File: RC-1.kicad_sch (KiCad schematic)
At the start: 0 parts

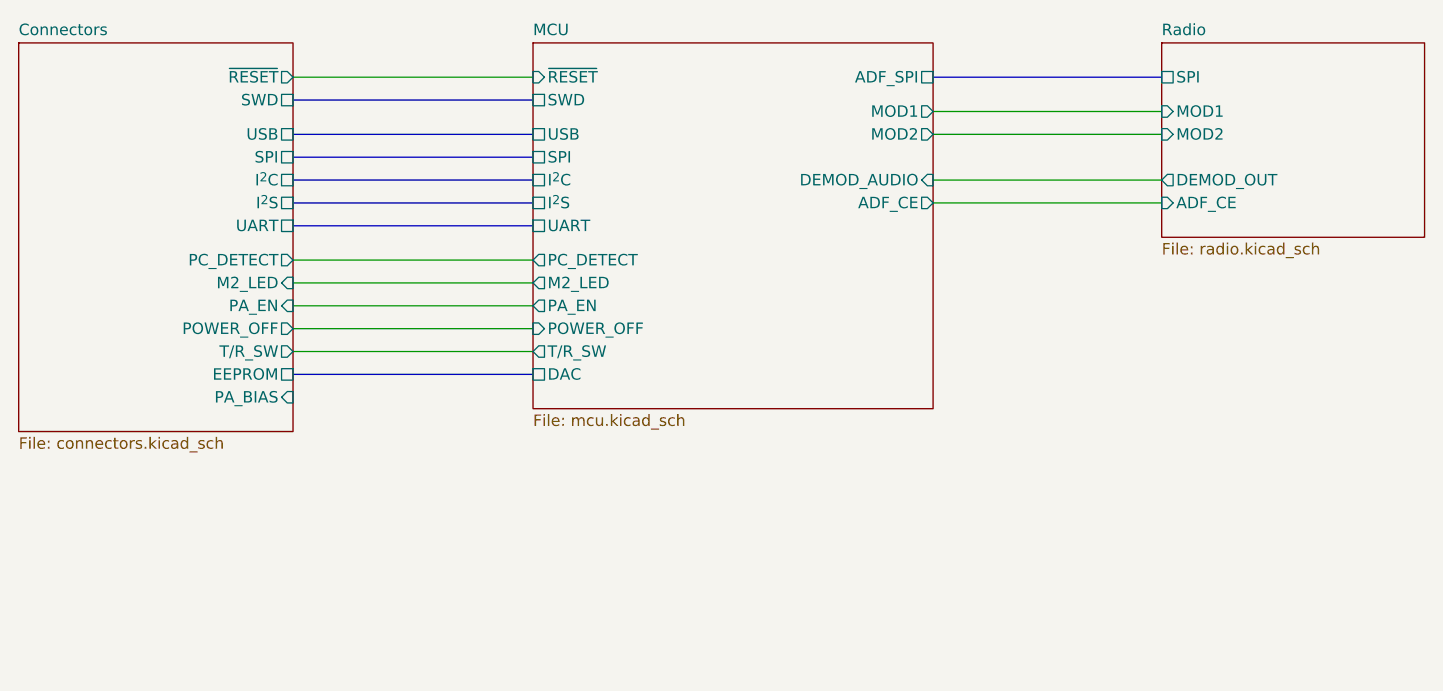
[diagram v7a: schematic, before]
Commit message: Added DAC for PA/preselector bias voltage
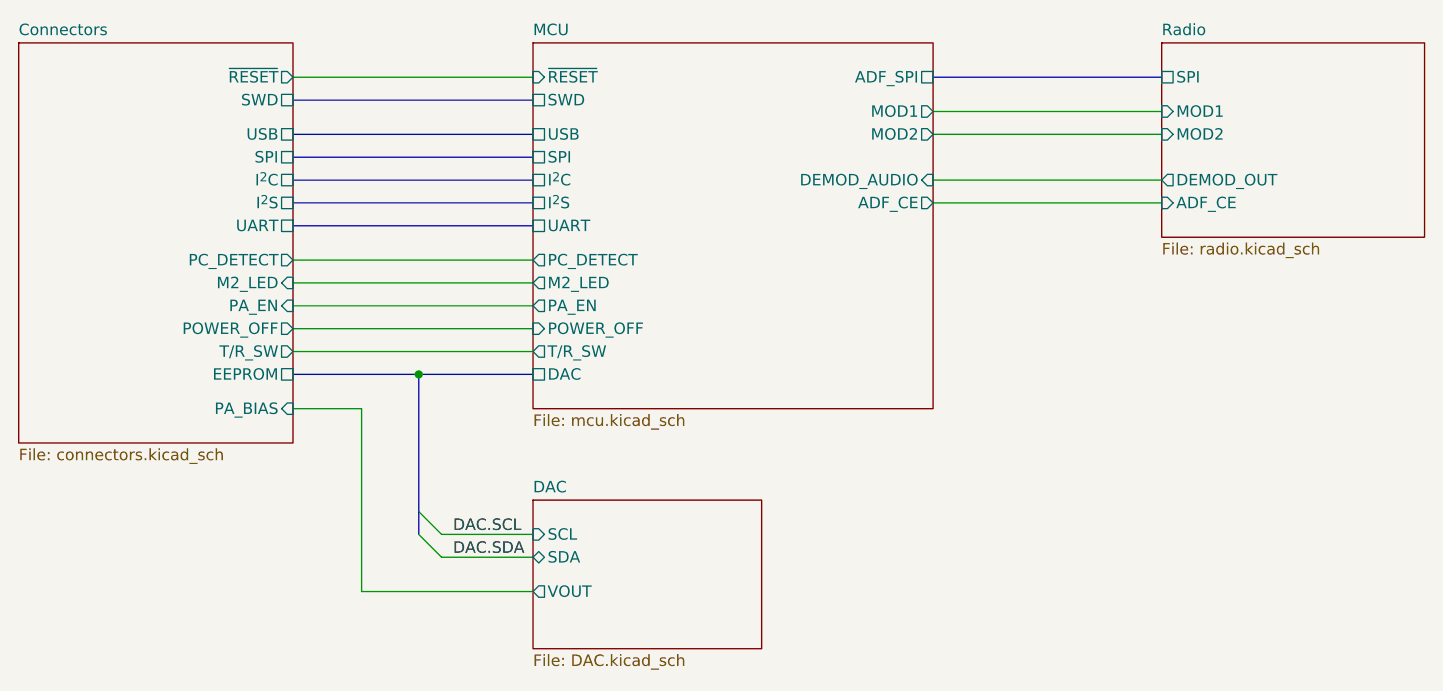
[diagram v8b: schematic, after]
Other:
- added sheet DAC (DAC.kicad_sch)
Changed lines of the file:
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@@
     (company "OpenRTX + M17")
   )
+  (junction (at 118.11 118.11) (diameter 0) (color 0 0 0 0)
+  )
+  (bus_entry (at 118.11 133.35) (size 2.54 2.54)
+    (stroke (width 0) (type default) (color 0 0 0 0))
+  )
+  (bus_entry (at 118.11 135.89) (size 2.54 2.54)
+    (stroke (width 0) (type default) (color 0 0 0 0))
+  )
   (bus (pts (xy 104.14 99.06) (xy 130.81 99.06))
     (stroke (width 0) (type default) (color 0 0 0 0))
   )
+  (wire (pts (xy 120.65 138.43) (xy 130.81 138.43))
+    (stroke (width 0) (type default) (color 0 0 0 0))
+  )
   (bus (pts (xy 104.14 87.63) (xy 130.81 87.63))
     (stroke (width 0) (type default) (color 0 0 0 0))
@@
     (stroke (width 0) (type default) (color 0 0 0 0))
   )
-  (bus (pts (xy 104.14 118.11) (xy 130.81 118.11))
+  (bus (pts (xy 104.14 118.11) (xy 118.11 118.11))
+    (stroke (width 0) (type default) (color 0 0 0 0))
+  )
+  (wire (pts (xy 111.76 121.92) (xy 111.76 142.24))
     (stroke (width 0) (type default) (color 0 0 0 0))
   )
@@
     (stroke (width 0) (type default) (color 0 0 0 0))
   )
+  (wire (pts (xy 111.76 142.24) (xy 130.81 142.24))
+    (stroke (width 0) (type default) (color 0 0 0 0))
+  )
   (wire (pts (xy 175.26 91.44) (xy 200.66 91.44))
     (stroke (width 0) (type default) (color 0 0 0 0))
@@
     (stroke (width 0) (type default) (color 0 0 0 0))
   )
+  (bus (pts (xy 118.11 118.11) (xy 130.81 118.11))
+    (stroke (width 0) (type default) (color 0 0 0 0))
+  )
+  (wire (pts (xy 120.65 135.89) (xy 130.81 135.89))
+    (stroke (width 0) (type default) (color 0 0 0 0))
+  )
+  (bus (pts (xy 118.11 133.35) (xy 118.11 135.89))
+    (stroke (width 0) (type default) (color 0 0 0 0))
+  )
   (bus (pts (xy 104.14 96.52) (xy 130.81 96.52))
     (stroke (width 0) (type default) (color 0 0 0 0))
   )
+  (bus (pts (xy 118.11 118.11) (xy 118.11 133.35))
+    (stroke (width 0) (type default) (color 0 0 0 0))
+  )
+  (wire (pts (xy 104.14 121.92) (xy 111.76 121.92))
+    (stroke (width 0) (type default) (color 0 0 0 0))
+  )
   (wire (pts (xy 104.14 85.09) (xy 130.81 85.09))
     (stroke (width 0) (type default) (color 0 0 0 0))
+  )
+  (label "DAC.SCL" (at 121.92 135.89 0)
+    (effects (font (size 1.27 1.27)) (justify left bottom))
+  )
+  (label "DAC.SDA" (at 121.92 138.43 0)
+    (effects (font (size 1.27 1.27)) (justify left bottom))
   )
   (sheet (at 130.81 81.28) (size 44.45 40.64) (fields_autoplaced)
@@
     )
   )
-  (sheet (at 73.66 81.28) (size 30.48 43.18) (fields_autoplaced)
+  (sheet (at 130.81 132.08) (size 25.4 16.51) (fields_autoplaced)
+    (stroke (width 0.1524) (type solid) (color 0 0 0 0))
+    (fill (color 0 0 0 0.0000))
+    (property "Sheet name" "DAC" (id 0) (at 130.81 131.3684 0)
+      (effects (font (size 1.27 1.27)) (justify left bottom))
+    )
+    (property "Sheet file" "DAC.kicad_sch" (id 1) (at 130.81 149.1746 0)
+      (effects (font (size 1.27 1.27)) (justify left top))
+    )
+    (pin "VOUT" output (at 130.81 142.24 180)
+      (effects (font (size 1.27 1.27)) (justify left))
+    )
+    (pin "SDA" bidirectional (at 130.81 138.43 180)
+      (effects (font (size 1.27 1.27)) (justify left))
+    )
+    (pin "SCL" input (at 130.81 135.89 180)
+      (effects (font (size 1.27 1.27)) (justify left))
+    )
+  )
+  (sheet (at 73.66 81.28) (size 30.48 44.45) (fields_autoplaced)
     (stroke (width 0.1524) (type solid) (color 0 0 0 0))
     (fill (color 0 0 0 0.0000))
@@
       (effects (font (size 1.27 1.27)) (justify left bottom))
     )
-    (property "Sheet file" "connectors.kicad_sch" (id 1) (at 73.66 125.0446 0)
+    (property "Sheet file" "connectors.kicad_sch" (id 1) (at 73.66 126.3146 0)
       (effects (font (size 1.27 1.27)) (justify left top))
     )
@@
       (effects (font (size 1.27 1.27)) (justify right))
     )
-    (pin "PA_BIAS" input (at 104.14 120.65 0)
+    (pin "PA_BIAS" input (at 104.14 121.92 0)
       (effects (font (size 1.27 1.27)) (justify right))
     )
@@
     (path "/37f64190-0af6-4571-a391-bfca4fb830ce" (page "3"))
     (path "/e9b5eb9e-a5da-44ea-89cf-1dbc5f8707b1" (page "4"))
+    (path "/68c6af70-3963-40f7-a571-68a1083177e1" (page "5"))
   )
   (symbol_instances
@@
       (reference "#PWR?") (unit 1) (value "GND") (footprint "")
     )
+    (path "/68c6af70-3963-40f7-a571-68a1083177e1/28717230-cde2-4374-9345-a50192a67a85"
+      (reference "#PWR?") (unit 1) (value "GND") (footprint "")
+    )
     (path "/e9b5eb9e-a5da-44ea-89cf-1dbc5f8707b1/2a6a8c96-9ee1-43a6-969f-063b295c4901"
       (reference "#PWR?") (unit 1) (value "GND") (footprint "")
@@
     (path "/e9b5eb9e-a5da-44ea-89cf-1dbc5f8707b1/2c4a4823-3df4-4715-82e4-ace04f59e52b"
       (reference "#PWR?") (unit 1) (value "GND") (footprint "")
+    )
+    (path "/68c6af70-3963-40f7-a571-68a1083177e1/2e16bdc6-1d41-4565-a5a9-5b22d0e93386"
+      (reference "#PWR?") (unit 1) (value "+3V3") (footprint "")
     )
     (path "/e9b5eb9e-a5da-44ea-89cf-1dbc5f8707b1/321442de-1be8-447c-864f-6a257a7c6538"
@@
       (reference "#PWR?") (unit 1) (value "GND") (footprint "")
     )
+    (path "/68c6af70-3963-40f7-a571-68a1083177e1/af86907f-c354-4f38-a850-1fb0ef968ac4"
+      (reference "#PWR?") (unit 1) (value "GND") (footprint "")
+    )
     (path "/d054b6a0-3a84-4aaa-901c-78f33fd51c3e/b2e1dedc-c0c0-4967-8a01-fc0733b70e7c"
       (reference "#PWR?") (unit 1) (value "GND") (footprint "")
@@
       (reference "C?") (unit 1) (value "100n") (footprint "Capacitor_SMD:C_0402_1005Metric")
     )
+    (path "/68c6af70-3963-40f7-a571-68a1083177e1/022057eb-7586-41e2-962c-49d840eb68d0"
+      (reference "C?") (unit 1) (value "100n") (footprint "Capacitor_SMD:C_0402_1005Metric")
+    )
     (path "/e9b5eb9e-a5da-44ea-89cf-1dbc5f8707b1/02c7f4e7-7551-498d-9164-07baed210898"
       (reference "C?") (unit 1) (value "15n") (footprint "Capacitor_SMD:C_0402_1005Metric")
@@
       (reference "C?") (unit 1) (value "100n") (footprint "Capacitor_SMD:C_0402_1005Metric")
     )
+    (path "/68c6af70-3963-40f7-a571-68a1083177e1/ab31a2b6-5416-47ce-a658-779ff6faeebe"
+      (reference "C?") (unit 1) (value "4.7μ") (footprint "Capacitor_SMD:C_0402_1005Metric")
+    )
     (path "/37f64190-0af6-4571-a391-bfca4fb830ce/b3a3f9da-f321-4d7a-a346-a6e1e8247570"
       (reference "C?") (unit 1) (value "100n") (footprint "Capacitor_SMD:C_0402_1005Metric")
@@
       (reference "U?") (unit 1) (value "ATSAMD51G19A-M") (footprint "Package_DFN_QFN:QFN-48-1EP_7x7mm_P0.5mm_EP5.15x5.15mm")
     )
+    (path "/68c6af70-3963-40f7-a571-68a1083177e1/66096f4f-c798-4425-8537-e7adeb21bec3"
+      (reference "U?") (unit 1) (value "DAC101C081CIMK") (footprint "Package_TO_SOT_SMD:SOT-23-6")
+    )
     (path "/e9b5eb9e-a5da-44ea-89cf-1dbc5f8707b1/129d23c4-4cbf-4d81-a95c-fb893f332360"
